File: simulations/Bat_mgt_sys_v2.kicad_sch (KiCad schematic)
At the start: 41 parts, among them Q1 PMOS, Q2 PMOS, U1 TLV76701DRVx, U2 MCP6561-OT, U4 74AHC1G02, U5 MCP6561-OT

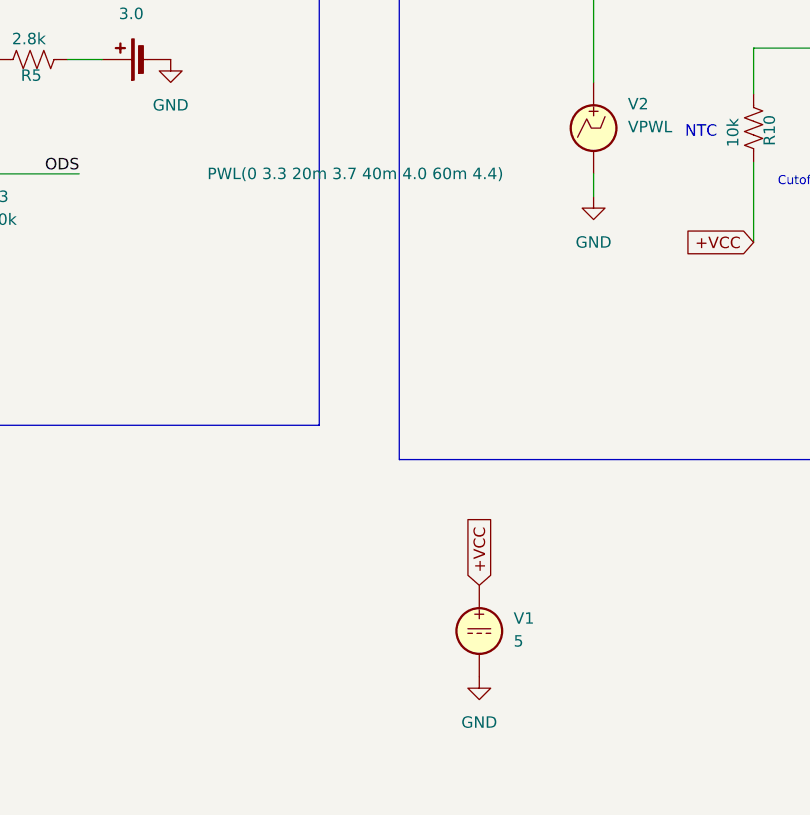
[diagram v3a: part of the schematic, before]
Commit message: check folder lm311 for comparator schematics
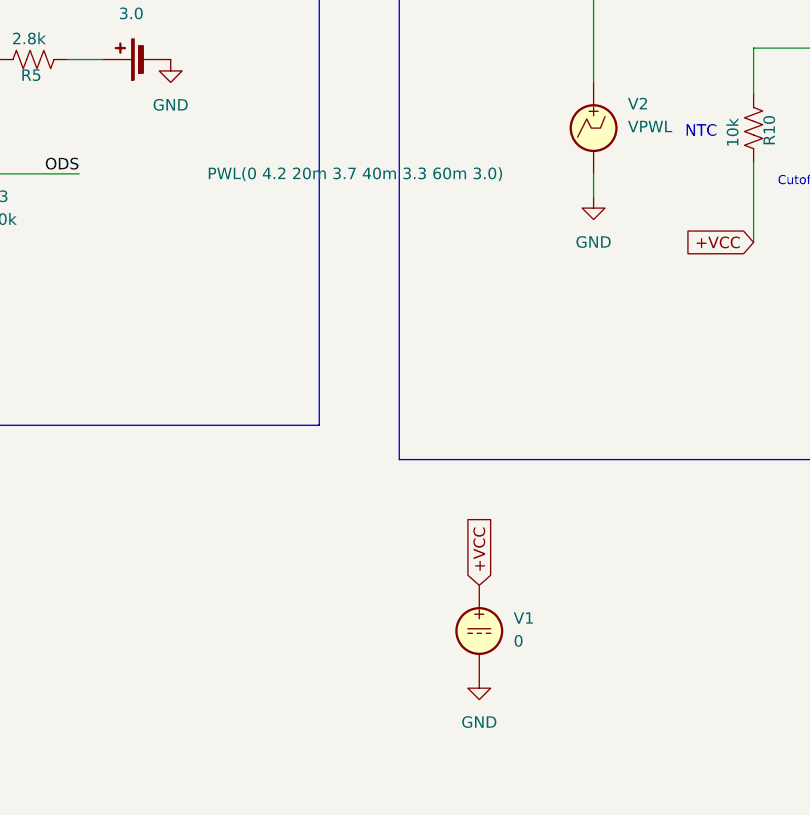
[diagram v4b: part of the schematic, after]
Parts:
- V1: value 5 -> 0
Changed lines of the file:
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@@
 			)
 		)
-		(property "Sim.Params" "PWL(0 3.3 20m 3.7 40m 4.0 60m 4.4)"
+		(property "Sim.Params" "PWL(0 4.2 20m 3.7 40m 3.3 60m 3.0)"
 			(at 169.164 176.53 0)
 			(show_name no)
@@
 			)
 		)
-		(property "Value" "5"
+		(property "Value" "0"
 			(at 203.2 228.4701 0)
 			(show_name no)
